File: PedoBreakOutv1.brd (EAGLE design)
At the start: 47 x 44.5 mm, 18 parts, among them IC1 LM1117MPX-2.85, J1 1050170001, J2 POWER_JACKSLT, J3 AVR_SPI_PROG_3X2NS, U1 ATTINY85-20P

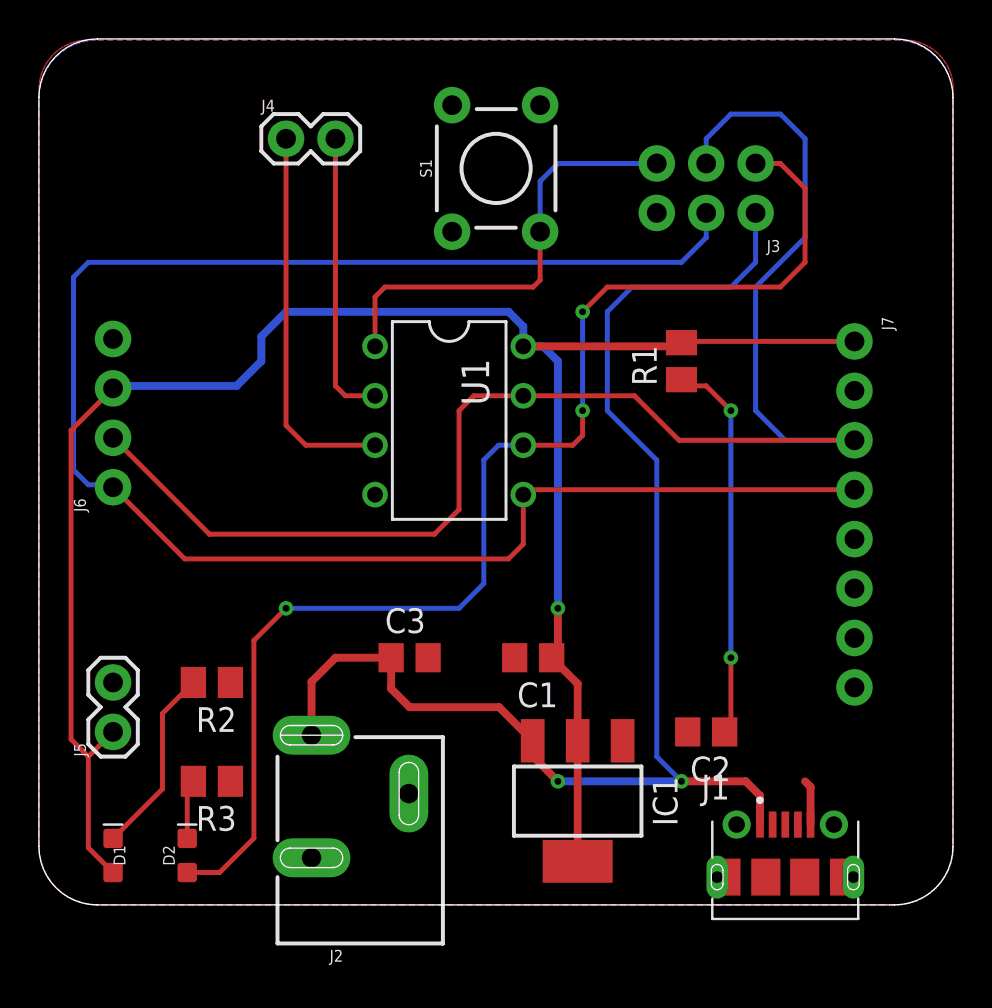
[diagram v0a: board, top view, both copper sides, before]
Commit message: Reduced size of board, removed ground plane issues
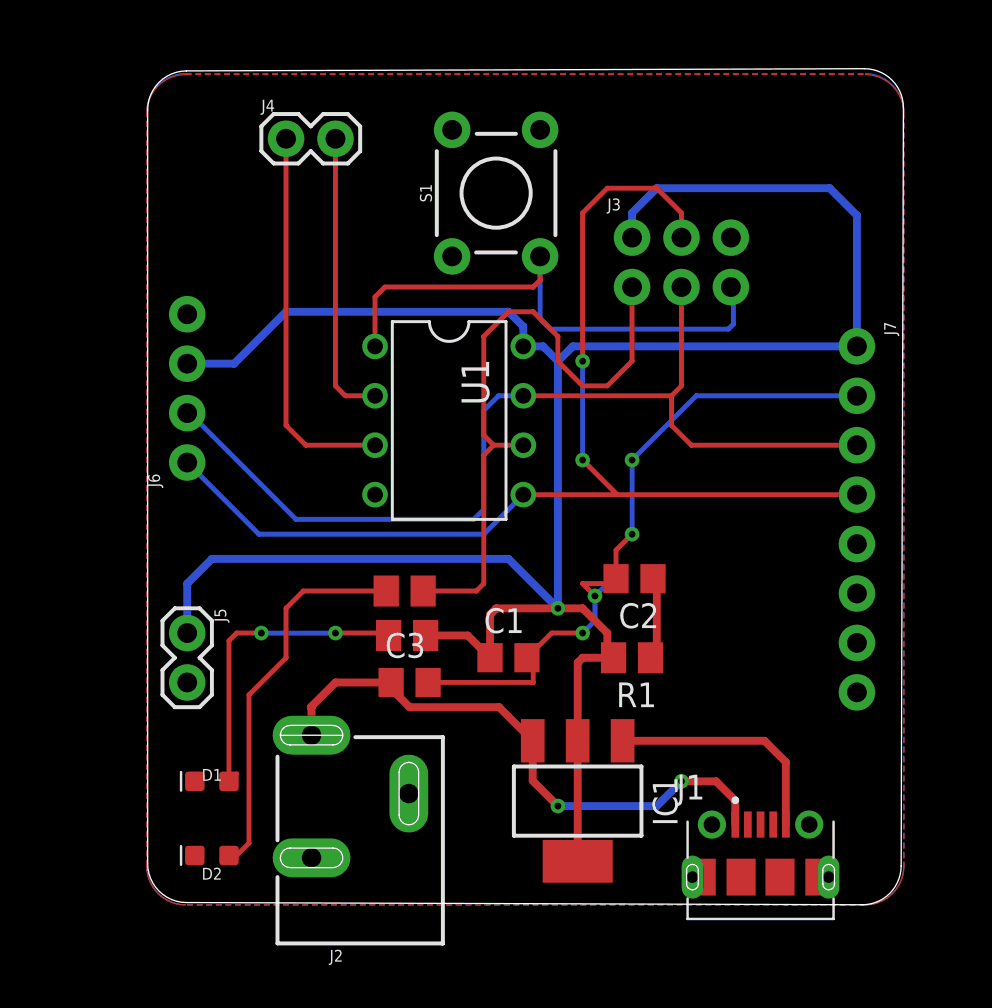
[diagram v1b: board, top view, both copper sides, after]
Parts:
- moved R1 15.5 mm to (35.6, 12.7), turned to 180 degrees
- moved R3 13.9 mm to (23.9, 16.1), turned to 0 degrees
- moved R2 10.3 mm to (24.0, 13.8), turned to 0 degrees
- moved C2 8.69 mm to (35.7, 16.8)
- moved D1 6.35 mm to (14.0, 6.35), turned to 180 degrees
- moved J5 6.35 mm to (12.7, 14.0), turned to 270 degrees
- moved J6 4.02 mm to (12.7, 22.7)
- moved J3 4.02 mm to (38.1, 33.0), turned to 0 degrees
- moved D2 1.27 mm to (14.0, 2.54), turned to 180 degrees
- moved C1 1.27 mm to (29.2, 12.7), turned to 0 degrees
- moved C3 1.27 mm to (24.1, 11.4)
- moved J1 1.27 mm to (42.2, 1.78)
- moved S1 1.27 mm to (28.6, 36.6)
- moved J7 0.28 mm to (47.1, 28.7)
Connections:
- net +3V3: now also J3.2, R2.2; no longer D1.A
- net GND: now also D1.C, D2.C; no longer R2.1, R3.1
- net MISO: now also R3.2; no longer D2.A
- net N$1: now also D1.A, R2.1; no longer D1.C, R2.2
- net N$3: now also D2.A, R3.1; no longer D2.C, R3.2
- net VIN: no longer J3.2
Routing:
- net GND: track 2.34 -> 47.4 mm, vias 0 -> 4
- net VIN: track 69.0 -> 30.0 mm
- net MISO: track 65.0 -> 33.0 mm, vias 3 -> 0
- net MOSI/SDA: track 89.5 -> 59.6 mm, vias 0 -> 2
- net SCK/SCL: track 75.2 -> 50.0 mm
- net +3V3: track 99.8 -> 120.3 mm
- net N$3: track 3.07 -> 19.7 mm
- net N$2: track 19.8 -> 4.46 mm, vias 2 -> 0
- net N$1: track 9.72 -> 16.2 mm, vias 0 -> 2
- net RST: track 22.8 -> 28.0 mm
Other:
- board size 47 x 44.5 mm -> 38.8 x 43 mm

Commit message: Added silkscreen logo, optimized GND plane
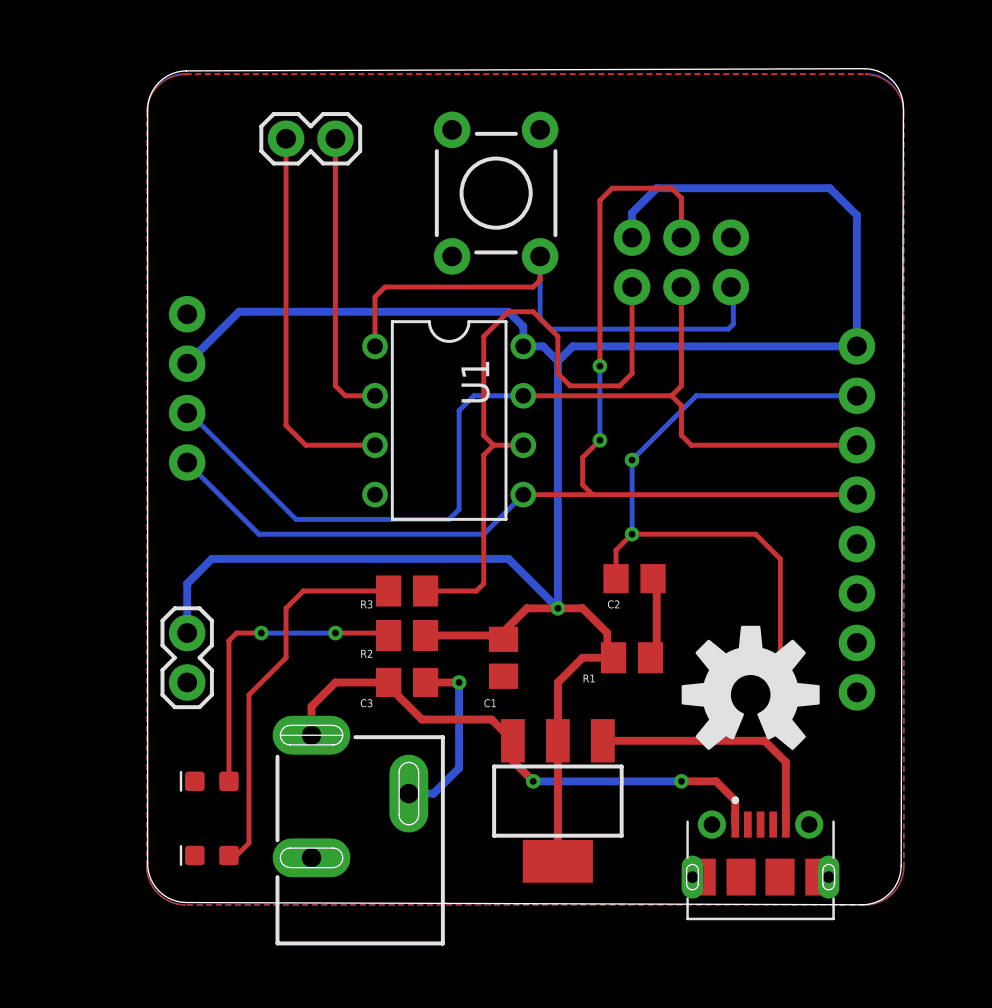
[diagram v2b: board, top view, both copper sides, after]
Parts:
- added U$1: (no value), SparkFun-Aesthetics:OSHW-LOGO-L
- moved IC1 1.02 mm to (31.8, 5.33)
- moved C1 0.25 mm to (29.0, 12.7), turned to 270 degrees
- moved C3 0.13 mm to (24.0, 11.4)
- moved R3 0.13 mm to (24.0, 16.1)
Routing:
- net GND: track 47.4 -> 59.9 mm, vias 4 -> 3
- net VIN: track 30.0 -> 28.2 mm
- net +3V3: track 120.3 -> 118.9 mm
- net N$1: track 16.2 -> 15.6 mm
- net MOSI/SDA: track 59.6 -> 59.0 mm
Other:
- board text added: "C1"
- board text added: "C2"
- board text added: "C3"
- board text added: "R1"
- board text added: "R2"
- board text added: "R3"
- board text added: "TinyPedometer v1.0 10/03/2020"

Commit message: Capacitor positioning, GND place modifications, aesthetics
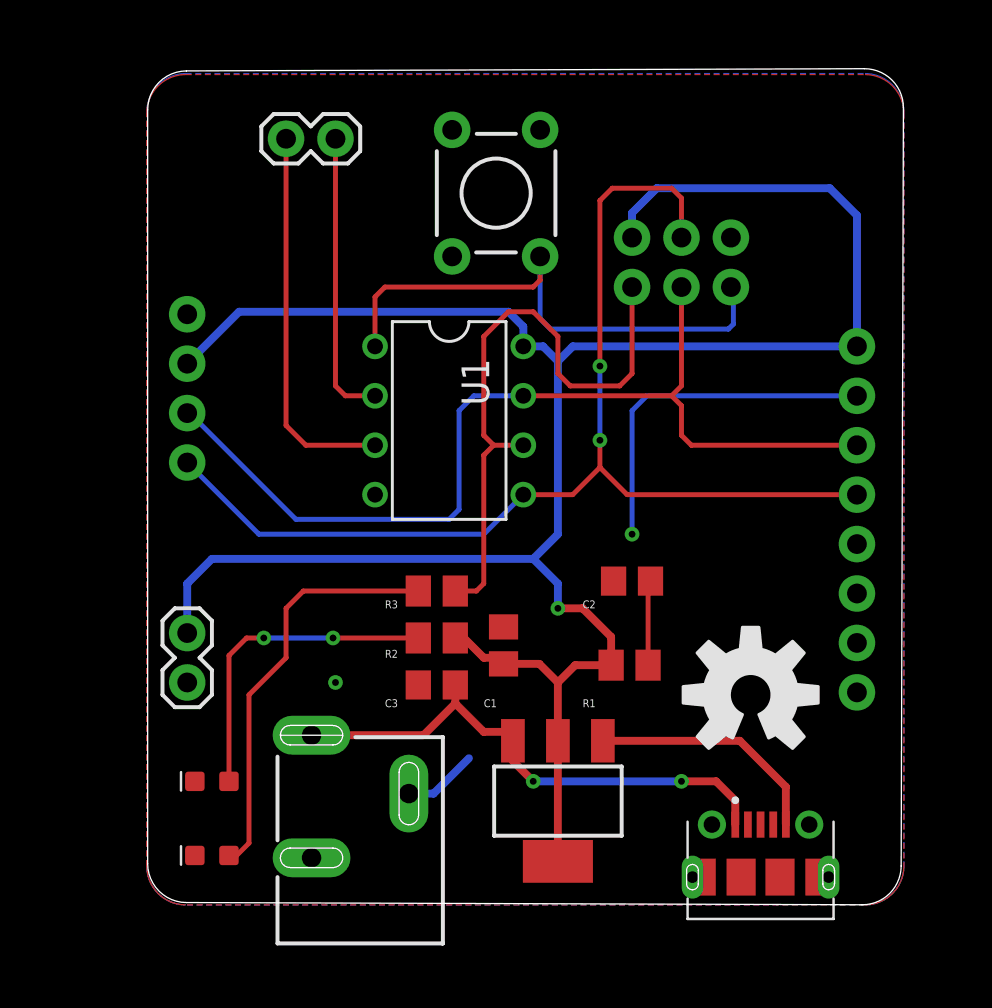
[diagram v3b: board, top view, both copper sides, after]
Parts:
- moved C3 1.53 mm to (25.5, 11.3), turned to 180 degrees
- moved R2 1.53 mm to (25.5, 13.7)
- moved R3 1.52 mm to (25.5, 16.1)
- moved C1 0.64 mm to (29.0, 13.3), turned to 90 degrees
- moved R1 0.40 mm to (35.4, 12.3)
- moved C2 0.18 mm to (35.6, 16.6)
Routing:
- net GND: track 59.9 -> 34.4 mm, vias 3 -> 2
- net +3V3: track 118.9 -> 116.1 mm
- net N$3: track 19.8 -> 21.3 mm
- net MISO: track 33.3 -> 31.8 mm
- net N$1: track 15.6 -> 16.6 mm
- net VIN: track 28.2 -> 27.5 mm
- net MOSI/SDA: track 59.0 -> 58.4 mm
